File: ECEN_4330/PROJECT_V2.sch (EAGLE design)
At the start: 22 parts

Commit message: Matched schematic with current breadboard config
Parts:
- 7SEGLATCH: value 74LS373N -> 74HC573N; device 74xx-us:74LS373N -> Fuckboiz:74HC573N
- DEMULTIPLEXER: value 74S373N -> 74AS573N; device 74xx-us:74S373N -> Fuckboiz:74AS573N
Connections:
- net 7SEGCSWR: now also 7SEGLATCHA.OC; no longer 7SEGLATCHA.ENC
- net ALE: now also DEMULTIPLEXERA.OC; no longer DEMULTIPLEXERA.ENC
- net GND: now also 7SEGLATCHA.C, DEMULTIPLEXERA.C; no longer 7SEGLATCHA.OC, DEMULTIPLEXERA.OC
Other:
- moved on the sheet: 7SEG, 7SEGLATCH

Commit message: Added LCD Circuit, Changed R/W Pin, Started ADC Circuit
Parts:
- added ADC: ADC, Fuckboiz:ADC
- added B, G, R: (no value), jumper:J2X5MM
- added LCD: (no value), Fuckboiz:LCD
- added R10: 3362P-1-103LF_POT, Fuckboiz:3362P-1-103LF_POT
- added TEMPSENS: TEMP_SENSOR, Fuckboiz:TEMP_SENSOR
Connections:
- new net N$16: LCD.VO, R10.2
- new net N$17: R.2
- new net N$2: G.2
- new net N$27: ADC.VCC
- new net N$28: ADC.GND
- new net N$32: LCD.R, R.1
- new net N$34: G.1, LCD.G
- new net N$36: B.1, LCD.B
- net A0: now also LCD.RS
- net ADCCS: now also ADC.!CS
- net D0: now also LCD.DB0
- net D1: now also ADC.D0, ADC.D1, LCD.DB1
- net D2: now also ADC.D2, LCD.DB2
- net D3: now also ADC.D3, LCD.DB3
- net D4: now also ADC.D4, LCD.DB4
- net D5: now also ADC.D5, LCD.DB5
- net D6: now also ADC.D6, LCD.DB6
- net D7: now also ADC.D7, LCD.DB7
- net GND: now also B.3, G.3, LCD.VDD, R.3, R10.1
- net LCDCS: now also LCD.EN
- net R/W: now also LCD.R/W~
- net RD: now also ADC.!RD
- net VCC: now also B.2, LCD.BL, LCD.VSS, R10.3
- net WR: now also ADC.!WR/RDY
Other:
- note added: "= neg-edge(RD, 1) neg-edge(WR, 0)"
- note added: "ADC"
- note added: "LCD"
- note added: "Latch?"
- note added: "W.I.P"
- note removed: "= ~RD + WR"

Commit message: Added RTC circuit
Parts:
- added RTC: (no value), Fuckboiz:RTC-72421
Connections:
- new net N$1: RTC.1
- new net N$23: RTC.3
- net A0: now also RTC.4
- net A1: now also RTC.5
- net A2: now also RTC.6
- net A3: now also RTC.7
- net D0: now also RTC.14
- net D1: now also RTC.13
- net D2: now also RTC.12
- net D3: now also RTC.11
- net GND: now also RTC.9
- net RD: now also RTC.8
- net RTCCS: now also RTC.2
- net VCC: now also RTC.15, RTC.16, RTC.17, RTC.18
- net WR: now also RTC.10
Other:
- note added: "Overall Circuit"
- note added: "RTC"

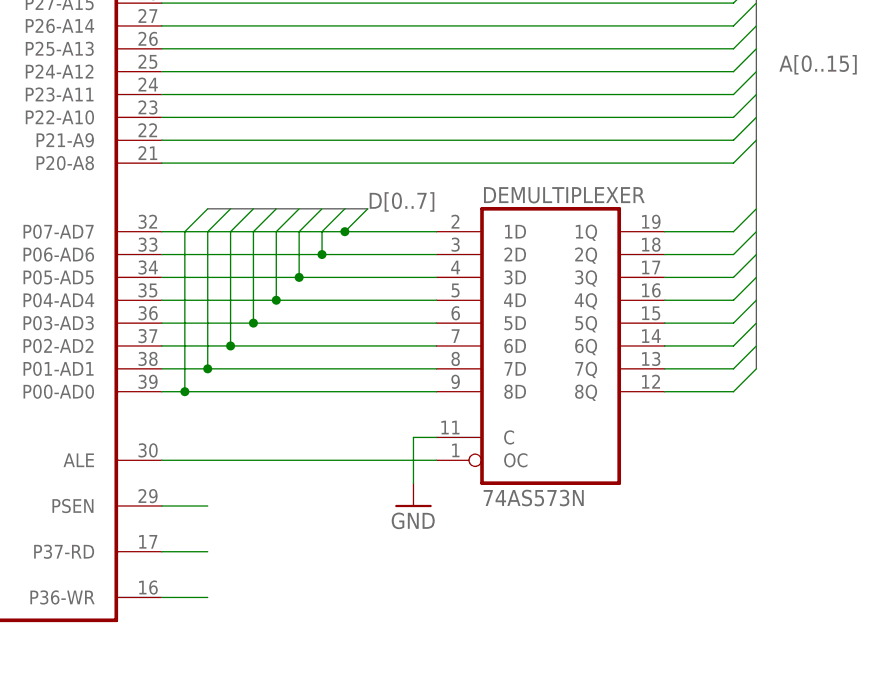
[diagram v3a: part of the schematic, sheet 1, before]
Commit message: Reverted chip_select, Fixed latch bug in schematic
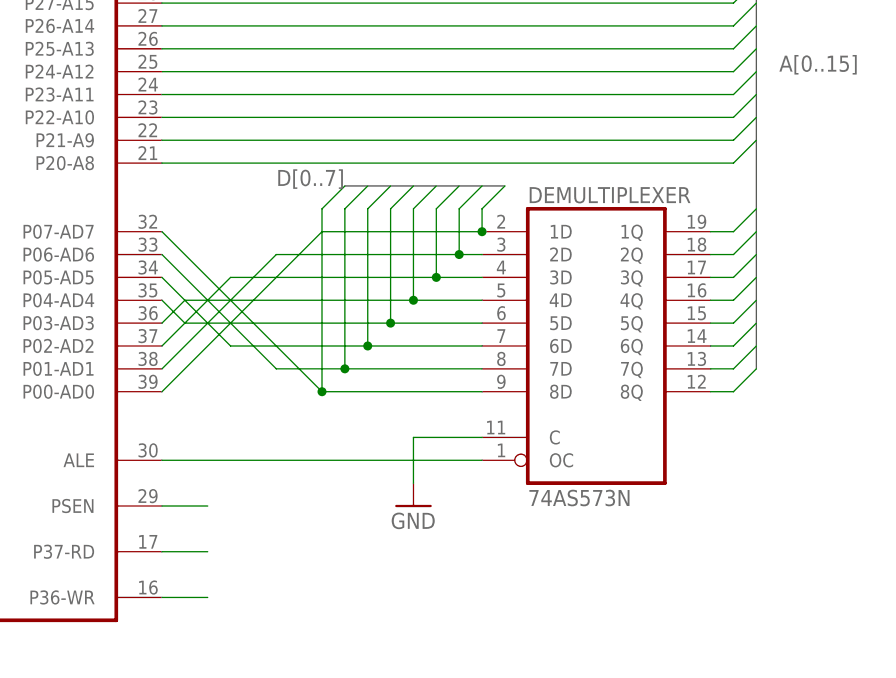
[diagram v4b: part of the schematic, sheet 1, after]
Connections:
- net 7SEGCSWR: now also 7SEGLATCHA.C; no longer 7SEGLATCHA.OC
- net A14: now also CSLOGICG$1.I2; no longer CSLOGICG$1.I1
- net A15: now also CSLOGICG$1.I1; no longer CSLOGICG$1.I0
- net D0: now also DEMULTIPLEXERA.1D; no longer DEMULTIPLEXERA.8D
- net D1: now also DEMULTIPLEXERA.2D; no longer DEMULTIPLEXERA.7D
- net D2: now also DEMULTIPLEXERA.3D; no longer DEMULTIPLEXERA.6D
- net D3: now also DEMULTIPLEXERA.4D; no longer DEMULTIPLEXERA.5D
- net D4: now also DEMULTIPLEXERA.5D; no longer DEMULTIPLEXERA.4D
- net D5: now also DEMULTIPLEXERA.6D; no longer DEMULTIPLEXERA.3D
- net D6: now also DEMULTIPLEXERA.7D; no longer DEMULTIPLEXERA.2D
- net D7: now also DEMULTIPLEXERA.8D; no longer DEMULTIPLEXERA.1D
- net GND: now also 7SEGLATCHA.OC; no longer 7SEGLATCHA.C
- net P3.5: now also CSLOGICG$1.I5; no longer CSLOGICG$1.I3
- net PSEN: now also CSLOGICG$1.I0; no longer CSLOGICG$1.I2
- net WR: now also CSLOGICG$1.I3; no longer CSLOGICG$1.I5
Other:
- note added: "= TBD"
- note removed: "= neg-edge(RD, 1) neg-edge(WR, 0)"
- moved on the sheet: DEMULTIPLEXER

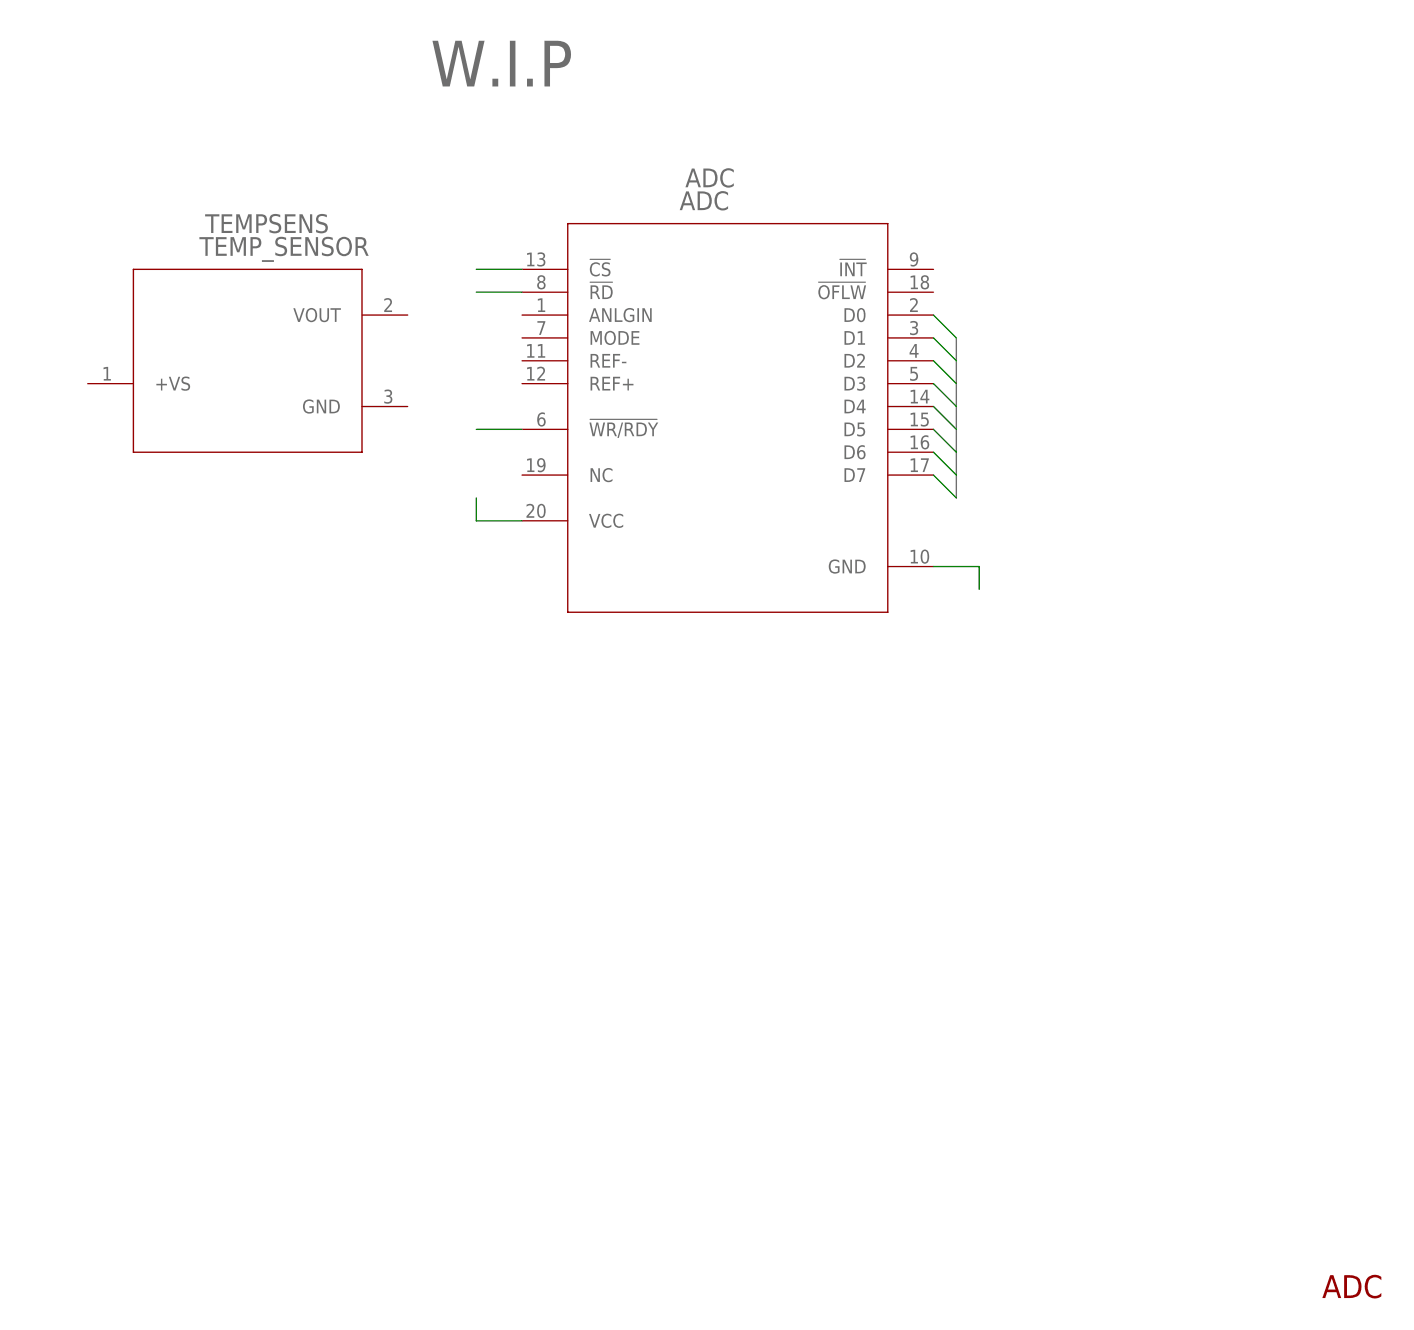
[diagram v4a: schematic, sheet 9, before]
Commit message: Added ADC to schematic, fixed other various 573 issues, Added LCD interfacing code to main
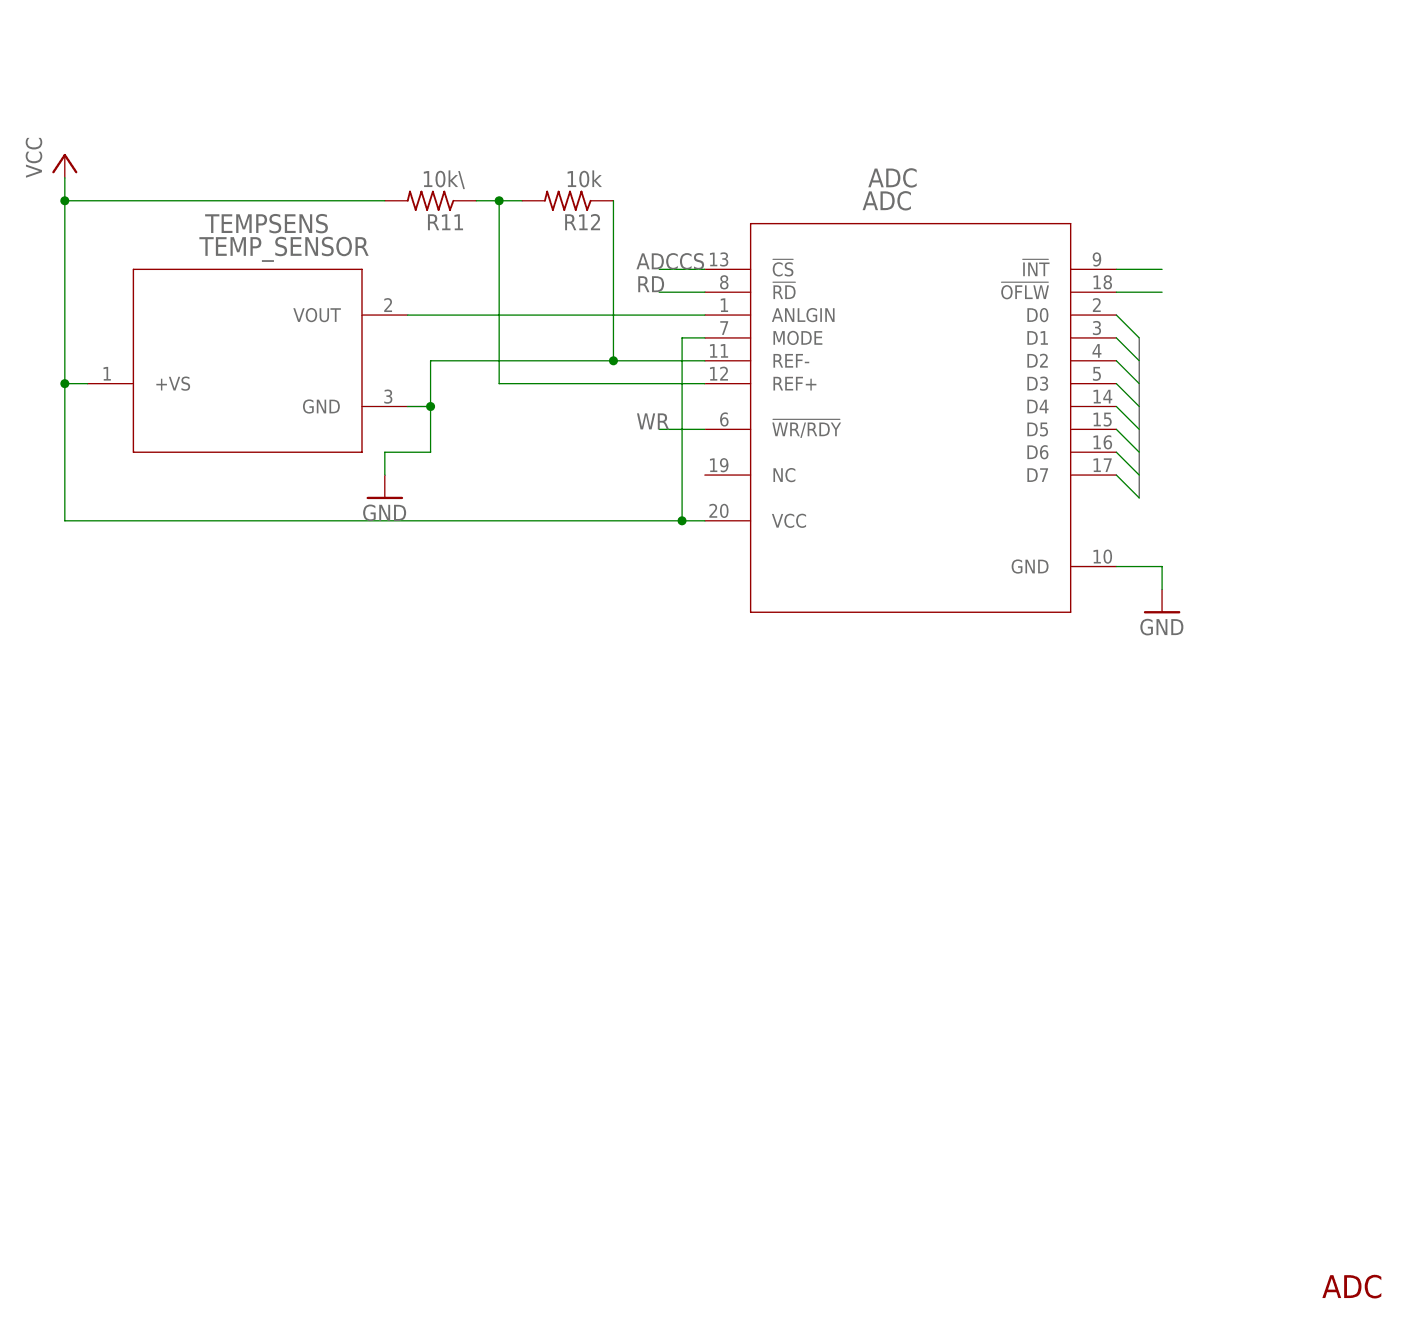
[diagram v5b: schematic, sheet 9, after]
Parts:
- added R11: 10k\, rcl:R-US_0204/5
- added R12: 10k, rcl:R-US_0204/5
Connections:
- removed net N$2: G.2
- removed net N$36: B.1, LCD.B
- new net N$26: ADC.ANLGIN, TEMPSENS.VOUT
- new net N$30: ADC.REF+, R11.1, R12.2
- net A1: now also LCD.R/W~
- net GND: now also ADC.GND, ADC.REF-, LCD.VSS, R12.1, TEMPSENS.GND; no longer LCD.VDD
- net N$17: now also B.2, LCD.B; no longer R.2
- net N$27: now also ADC.!INT; no longer ADC.VCC
- net N$28: now also ADC.!OFLW; no longer ADC.GND
- net N$32: now also R.2; no longer R.1
- net N$34: now also G.2; no longer G.1
- net R/W: no longer LCD.R/W~
- net VCC: now also ADC.MODE, ADC.VCC, B.1, G.1, LCD.VDD, R.1, R11.2, TEMPSENS.+VS; no longer B.2, LCD.VSS
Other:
- note removed: "W.I.P"
- moved on the sheet: ADC

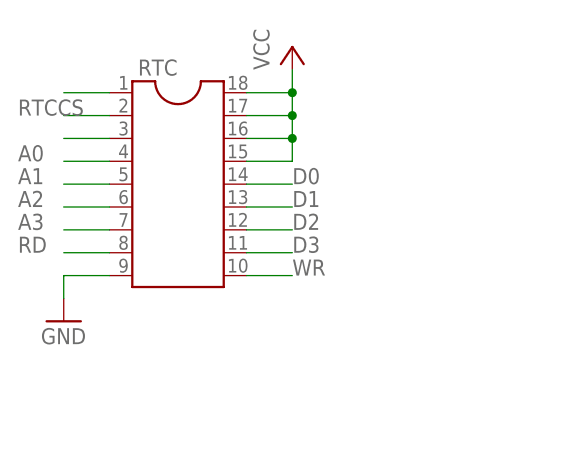
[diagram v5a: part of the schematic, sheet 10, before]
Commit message: Added RTC, LCD, ADC Code
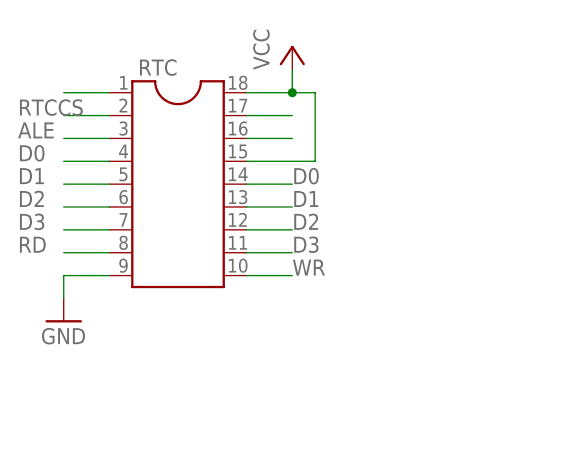
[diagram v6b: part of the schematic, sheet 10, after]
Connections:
- removed net N$23: RTC.3
- new net N$25: RTC.16
- new net N$29: RTC.17
- net A0: no longer RTC.4
- net A1: no longer RTC.5
- net A2: no longer RTC.6
- net A3: no longer RTC.7
- net ALE: now also RTC.3
- net D0: now also RTC.4
- net D1: now also RTC.5
- net D2: now also RTC.6
- net D3: now also RTC.7
- net VCC: no longer RTC.16, RTC.17
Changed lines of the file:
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@@
 </segment>
 </net>
-<net name="N$23" class="0">
+<net name="ALE" class="0">
 <segment>
 <pinref part="RTC" gate="G$1" pin="3"/>
 <wire x1="20.32" y1="165.1" x2="15.24" y2="165.1" width="0.1524" layer="91"/>
-</segment>
-</net>
-<net name="A0" class="0">
-<segment>
-<pinref part="RTC" gate="G$1" pin="4"/>
-<wire x1="20.32" y1="162.56" x2="15.24" y2="162.56" width="0.1524" layer="91"/>
-<label x="10.16" y="162.56" size="1.778" layer="95"/>
-</segment>
-</net>
-<net name="A1" class="0">
-<segment>
-<pinref part="RTC" gate="G$1" pin="5"/>
-<wire x1="20.32" y1="160.02" x2="15.24" y2="160.02" width="0.1524" layer="91"/>
-<label x="10.16" y="160.02" size="1.778" layer="95"/>
-</segment>
-</net>
-<net name="A2" class="0">
-<segment>
-<pinref part="RTC" gate="G$1" pin="6"/>
-<wire x1="20.32" y1="157.48" x2="15.24" y2="157.48" width="0.1524" layer="91"/>
-<label x="10.16" y="157.48" size="1.778" layer="95"/>
-</segment>
-</net>
-<net name="A3" class="0">
-<segment>
-<pinref part="RTC" gate="G$1" pin="7"/>
-<wire x1="20.32" y1="154.94" x2="15.24" y2="154.94" width="0.1524" layer="91"/>
-<label x="10.16" y="154.94" size="1.778" layer="95"/>
+<label x="10.16" y="165.1" size="1.778" layer="95"/>
 </segment>
 </net>
@@
 <label x="40.64" y="152.4" size="1.778" layer="95"/>
 </segment>
+<segment>
+<pinref part="RTC" gate="G$1" pin="7"/>
+<wire x1="20.32" y1="154.94" x2="15.24" y2="154.94" width="0.1524" layer="91"/>
+<label x="10.16" y="154.94" size="1.778" layer="95"/>
+</segment>
 </net>
 <net name="D2" class="0">
@@
 <wire x1="35.56" y1="154.94" x2="40.64" y2="154.94" width="0.1524" layer="91"/>
 <label x="40.64" y="154.94" size="1.778" layer="95"/>
+</segment>
+<segment>
+<pinref part="RTC" gate="G$1" pin="6"/>
+<wire x1="20.32" y1="157.48" x2="15.24" y2="157.48" width="0.1524" layer="91"/>
+<label x="10.16" y="157.48" size="1.778" layer="95"/>
 </segment>
 </net>
@@
 <label x="40.64" y="157.48" size="1.778" layer="95"/>
 </segment>
+<segment>
+<pinref part="RTC" gate="G$1" pin="5"/>
+<wire x1="20.32" y1="160.02" x2="15.24" y2="160.02" width="0.1524" layer="91"/>
+<label x="10.16" y="160.02" size="1.778" layer="95"/>
+</segment>
 </net>
 <net name="D0" class="0">
@@
 <label x="40.64" y="160.02" size="1.778" layer="95"/>
 </segment>
+<segment>
+<pinref part="RTC" gate="G$1" pin="4"/>
+<wire x1="20.32" y1="162.56" x2="15.24" y2="162.56" width="0.1524" layer="91"/>
+<label x="10.16" y="162.56" size="1.778" layer="95"/>
+</segment>
 </net>
 <net name="VCC" class="0">
 <segment>
-<pinref part="RTC" gate="G$1" pin="16"/>
-<wire x1="35.56" y1="165.1" x2="40.64" y2="165.1" width="0.1524" layer="91"/>
-<pinref part="RTC" gate="G$1" pin="17"/>
-<wire x1="35.56" y1="167.64" x2="40.64" y2="167.64" width="0.1524" layer="91"/>
-<wire x1="40.64" y1="165.1" x2="40.64" y2="167.64" width="0.1524" layer="91"/>
 <pinref part="RTC" gate="G$1" pin="18"/>
 <wire x1="35.56" y1="170.18" x2="40.64" y2="170.18" width="0.1524" layer="91"/>
-<wire x1="40.64" y1="167.64" x2="40.64" y2="170.18" width="0.1524" layer="91"/>
-<junction x="40.64" y="167.64"/>
 <wire x1="40.64" y1="170.18" x2="40.64" y2="172.72" width="0.1524" layer="91"/>
+<pinref part="P+9" gate="VCC" pin="VCC"/>
+<pinref part="RTC" gate="G$1" pin="15"/>
+<wire x1="35.56" y1="162.56" x2="43.18" y2="162.56" width="0.1524" layer="91"/>
+<wire x1="43.18" y1="162.56" x2="43.18" y2="170.18" width="0.1524" layer="91"/>
+<wire x1="43.18" y1="170.18" x2="40.64" y2="170.18" width="0.1524" layer="91"/>
 <junction x="40.64" y="170.18"/>
-<pinref part="RTC" gate="G$1" pin="15"/>
-<wire x1="35.56" y1="162.56" x2="40.64" y2="162.56" width="0.1524" layer="91"/>
-<wire x1="40.64" y1="162.56" x2="40.64" y2="165.1" width="0.1524" layer="91"/>
-<junction x="40.64" y="165.1"/>
-<pinref part="P+9" gate="VCC" pin="VCC"/>
 </segment>
 </net>
@@
 </segment>
 </net>
+<net name="N$25" class="0">
+<segment>
+<pinref part="RTC" gate="G$1" pin="16"/>
+<wire x1="35.56" y1="165.1" x2="40.64" y2="165.1" width="0.1524" layer="91"/>
+</segment>
+</net>
+<net name="N$29" class="0">
+<segment>
+<pinref part="RTC" gate="G$1" pin="17"/>
+<wire x1="35.56" y1="167.64" x2="40.64" y2="167.64" width="0.1524" layer="91"/>
+</segment>
+</net>
